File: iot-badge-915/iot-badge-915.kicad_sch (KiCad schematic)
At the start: 73 parts, among them J1 USB_C_Receptacle_USB2.0, J2 Wire ANT, J3 Conn_01x04_Male, Q1 BC847, Q2 BC847, SW1 SW_Push, SW2 SW_Push, SW3 SW_Push, SW4 SW_Push, SW5 SW_Push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

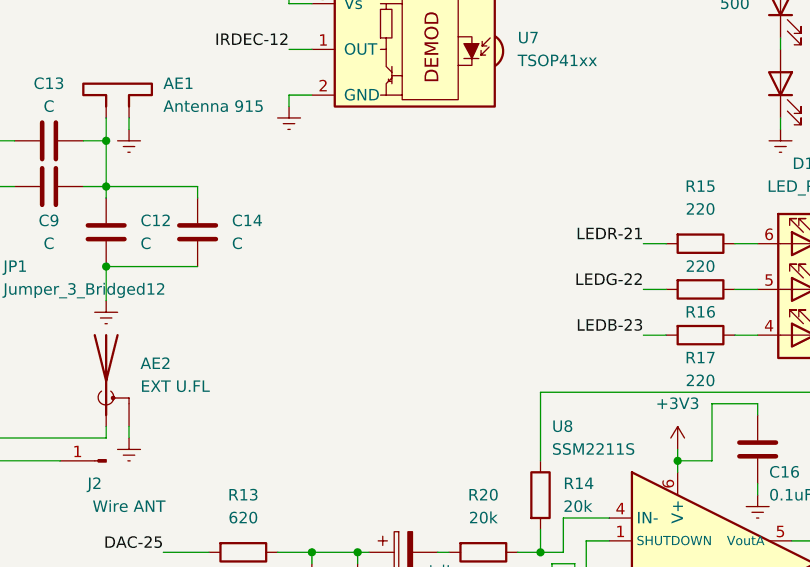
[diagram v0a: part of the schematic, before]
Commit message: added i2s mic symbol
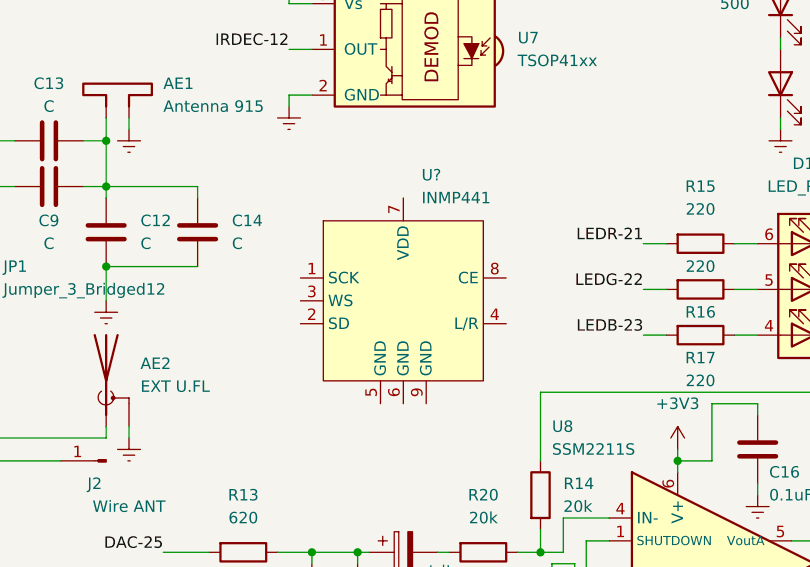
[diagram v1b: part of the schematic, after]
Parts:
- added U?: INMP441, symbol Microphone_I2S:INMP441
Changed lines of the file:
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@@
     (effects (font (size 1.27 1.27)) (justify left bottom))
+  )
+  (symbol (lib_id "Microphone_I2S:INMP441") (at 214.63 92.71 0) (unit 1)
+    (in_bom yes) (on_board yes) (fields_autoplaced)
+    (property "Reference" "U?" (id 0) (at 216.6494 78.74 0)
+      (effects (font (size 1.27 1.27)) (justify left))
+    )
+    (property "Value" "INMP441" (id 1) (at 216.6494 81.28 0)
+      (effects (font (size 1.27 1.27)) (justify left))
+    )
+    (property "Footprint" "" (id 2) (at 214.63 92.71 0)
+      (effects (font (size 1.27 1.27)) hide)
+    )
+    (property "Datasheet" "" (id 3) (at 214.63 92.71 0)
+      (effects (font (size 1.27 1.27)) hide)
+    )
+    (pin "1")
+    (pin "2")
+    (pin "3")
+    (pin "4")
+    (pin "5")
+    (pin "6")
+    (pin "7")
+    (pin "8")
+    (pin "9")
   )
   (symbol (lib_id "power:Earth") (at 46.99 189.23 0) (unit 1)
@@
       (reference "U8") (unit 1) (value "SSM2211S") (footprint "Package_SO:SOIC-8_3.9x4.9mm_P1.27mm")
     )
+    (path "/0027f7de-2de1-4926-a80b-a6847e3b308a"
+      (reference "U?") (unit 1) (value "INMP441") (footprint "")
+    )
     (path "/b6bf3229-edbf-4e20-84e4-316f6abc0502"

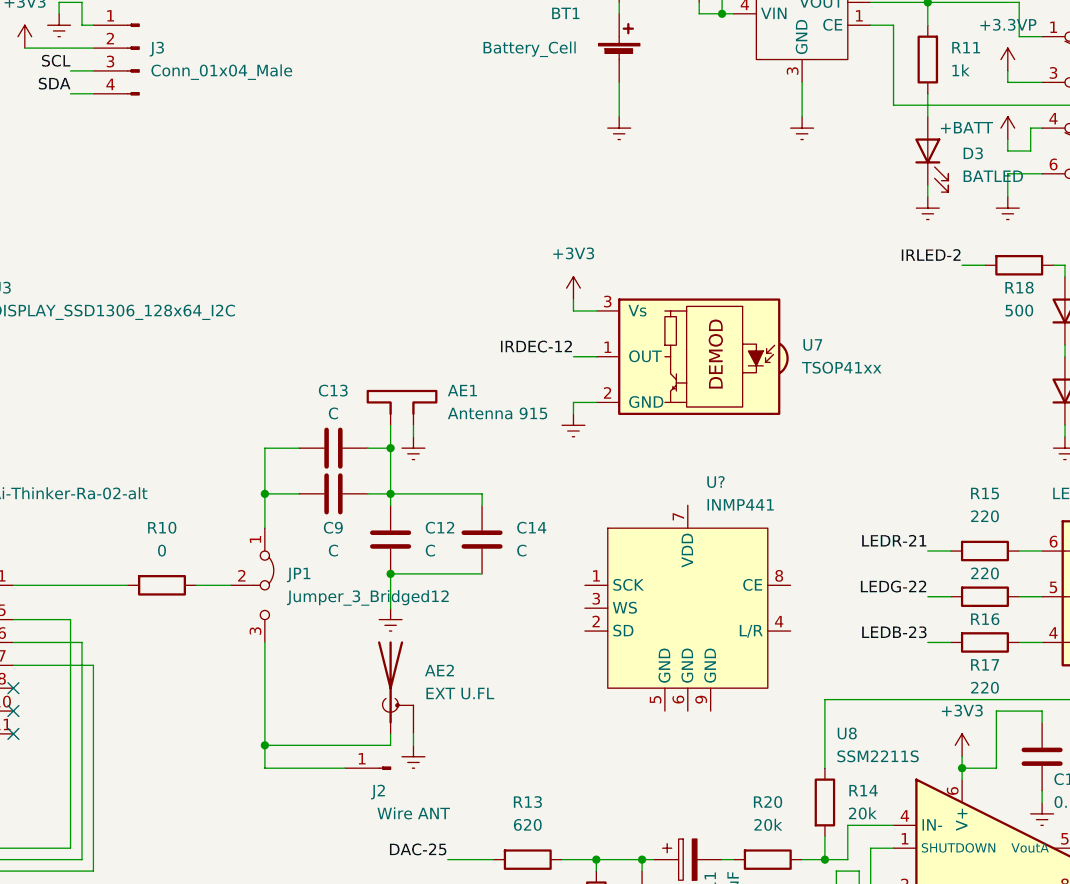
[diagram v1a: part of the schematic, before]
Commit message: placed i2c mic in pcb
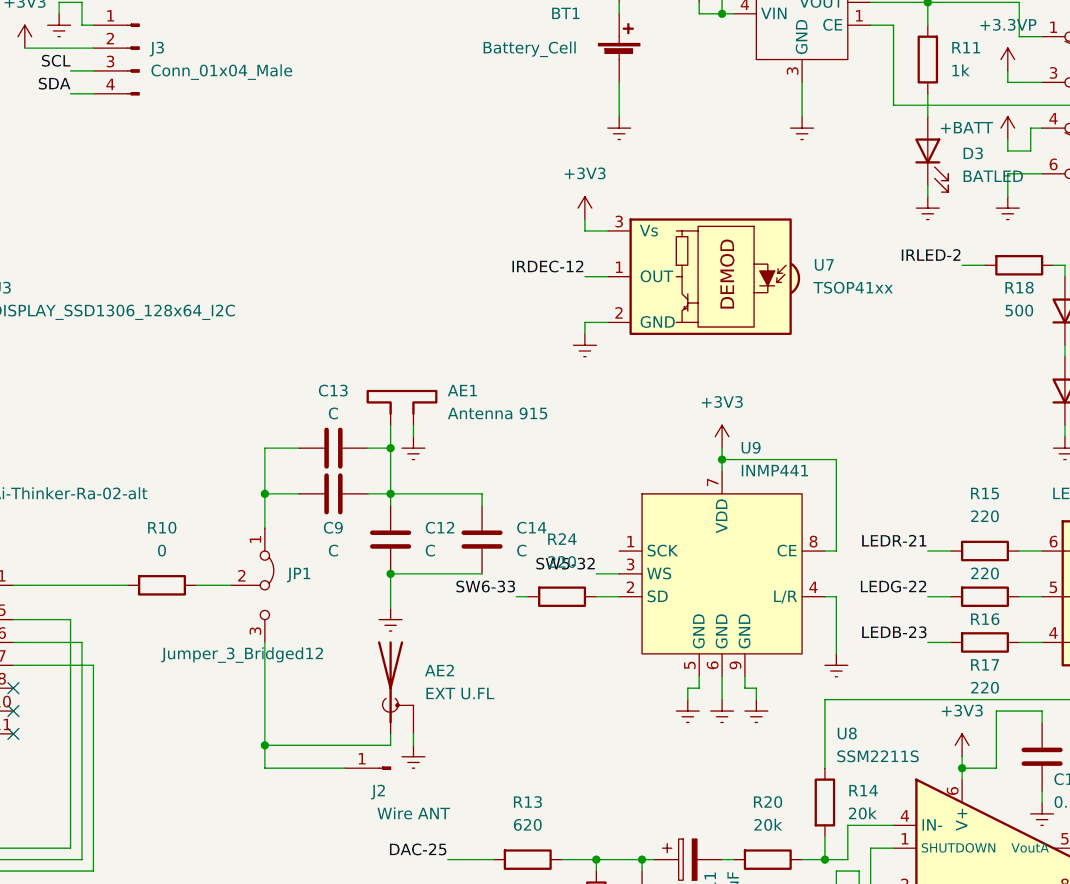
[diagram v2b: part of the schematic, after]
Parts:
- added R24: 220, Resistor_SMD:R_0805_2012Metric_Pad1.20x1.40mm_HandSolder, symbol Device:R
- U9: renamed from U?; footprint (none) -> Microphone_I2S:INMP441
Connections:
- net +3V3: now also U9.7 (VDD), U9.8 (CE)
- net Earth: now also U9.4 (L/R), U9.5 (GND), U9.6 (GND), U9.9 (GND)
- net SW5-32: now also U9.3 (WS)
- net SW6-33: now also R24.2
- net at U9.2 (SD): now also R24.1
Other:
- moved on the sheet: U7, U9

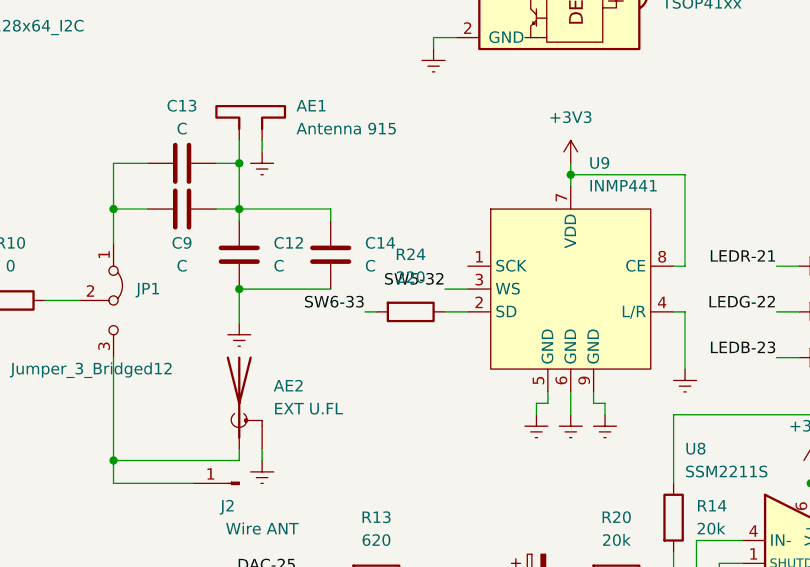
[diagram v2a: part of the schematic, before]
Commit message: finished placing i2s mic
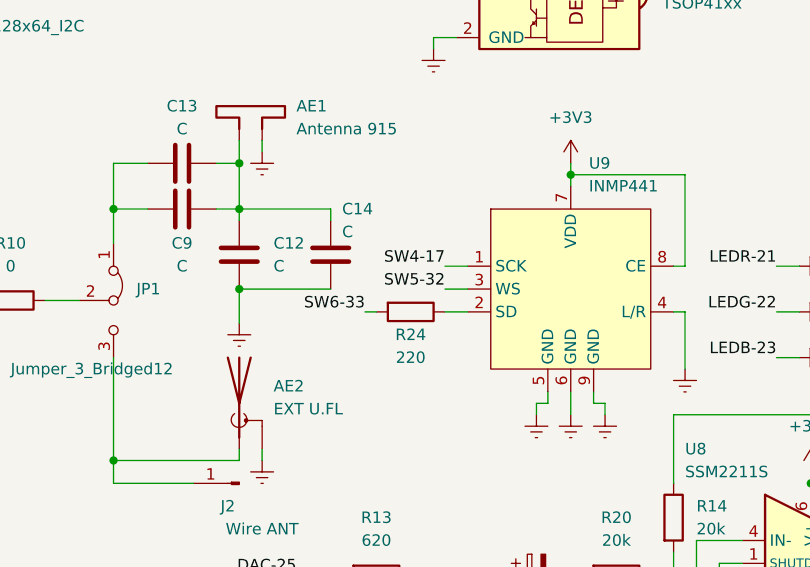
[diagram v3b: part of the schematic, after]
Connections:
- net SW4-17: now also U9.1 (SCK)
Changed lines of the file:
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@@
+    (stroke (width 0) (type default) (color 0 0 0 0))
+  )
+  (wire (pts (xy 204.47 86.36) (xy 207.01 86.36))
     (stroke (width 0) (type default) (color 0 0 0 0))
   )
@@
   )
   (label "SW3-16" (at 217.17 146.05 180)
+    (effects (font (size 1.27 1.27)) (justify right bottom))
+  )
+  (label "SW4-17" (at 204.47 86.36 180)
     (effects (font (size 1.27 1.27)) (justify right bottom))
   )
@@
   )
   (symbol (lib_id "Device:C") (at 191.77 85.09 180) (unit 1)
-    (in_bom yes) (on_board yes) (fields_autoplaced)
-    (property "Reference" "C14" (id 0) (at 195.58 83.8199 0)
+    (in_bom yes) (on_board yes)
+    (property "Reference" "C14" (id 0) (at 193.04 80.01 0)
       (effects (font (size 1.27 1.27)) (justify right))
     )
-    (property "Value" "C" (id 1) (at 195.58 86.3599 0)
+    (property "Value" "C" (id 1) (at 193.04 82.55 0)
       (effects (font (size 1.27 1.27)) (justify right))
     )
@@
   )
   (symbol (lib_id "Device:R") (at 200.66 91.44 270) (unit 1)
-    (in_bom yes) (on_board yes) (fields_autoplaced)
-    (property "Reference" "R24" (id 0) (at 200.66 85.09 90))
-    (property "Value" "220" (id 1) (at 200.66 87.63 90))
+    (in_bom yes) (on_board yes)
+    (property "Reference" "R24" (id 0) (at 200.66 93.98 90))
+    (property "Value" "220" (id 1) (at 200.66 96.52 90))
     (property "Footprint" "Resistor_SMD:R_0805_2012Metric_Pad1.20x1.40mm_HandSolder" (id 2) (at 200.66 89.662 90)
       (effects (font (size 1.27 1.27)) hide)
